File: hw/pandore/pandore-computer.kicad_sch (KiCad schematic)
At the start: 0 parts

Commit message: Added lots to sch and pcb: eth passive, audio codec, midi, teensy Corrected and added support for M.2
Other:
- sheet Computer module ports: added PCIEP0{PCIE1X}, PCIEP1{PCIE1X}, PCIEP2{PCIE1X}, PCIEP3{PCIE4X}, UART0{UART}, UART1{UART}, UART2{UART}; removed none
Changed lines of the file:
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@@
+		)
+	)
+	(wire
+		(pts
+			(xy 215.9 124.46) (xy 165.1 124.46)
+		)
+		(stroke
+			(width 0)
+			(type default)
 		)
 	)
@@
 		)
 	)
+	(wire
+		(pts
+			(xy 215.9 121.92) (xy 165.1 121.92)
+		)
+		(stroke
+			(width 0)
+			(type default)
+		)
+	)
 	(bus
 		(pts
@@
 		)
 	)
+	(wire
+		(pts
+			(xy 215.9 127) (xy 165.1 127)
+		)
+		(stroke
+			(width 0)
+			(type default)
+		)
+	)
+	(bus
+		(pts
+			(xy 92.71 140.97) (xy 121.92 140.97)
+		)
+		(stroke
+			(width 0)
+			(type default)
+		)
+	)
 	(bus
 		(pts
@@
 		)
 	)
+	(wire
+		(pts
+			(xy 215.9 119.38) (xy 165.1 119.38)
+		)
+		(stroke
+			(width 0)
+			(type default)
+		)
+	)
 	(bus
 		(pts
@@
 		(shape bidirectional)
 		(at 215.9 96.52 0)
+		(effects
+			(font
+				(size 1.016 1.016)
+			)
+			(justify left)
+		)
+	)
+	(hierarchical_label "M2E{PCIE1X}"
+		(shape bidirectional)
+		(at 215.9 121.92 0)
 		(effects
 			(font
@@
 		)
 	)
+	(hierarchical_label "ETHX{PCIE1X}"
+		(shape bidirectional)
+		(at 215.9 124.46 0)
+		(effects
+			(font
+				(size 1.016 1.016)
+			)
+			(justify left)
+		)
+	)
 	(hierarchical_label "DDIB{HDMI}"
 		(shape output)
@@
 		)
 	)
+	(hierarchical_label "MIDI{UART}"
+		(shape bidirectional)
+		(at 92.71 140.97 180)
+		(effects
+			(font
+				(size 1.016 1.016)
+			)
+			(justify right)
+		)
+	)
+	(hierarchical_label "M2M{PCIE4X}"
+		(shape bidirectional)
+		(at 215.9 127 0)
+		(effects
+			(font
+				(size 1.016 1.016)
+			)
+			(justify left)
+		)
+	)
 	(hierarchical_label "USBP1{USB3}"
 		(shape bidirectional)
 		(at 215.9 93.98 0)
+		(effects
+			(font
+				(size 1.016 1.016)
+			)
+			(justify left)
+		)
+	)
+	(hierarchical_label "ETHI{PCIE1X}"
+		(shape bidirectional)
+		(at 215.9 119.38 0)
 		(effects
 			(font
@@
 			)
 		)
+		(pin "PCIEP3{PCIE4X}" bidirectional
+			(at 165.1 127 0)
+			(effects
+				(font
+					(size 1.016 1.016)
+				)
+				(justify right)
+			)
+		)
+		(pin "PCIEP2{PCIE1X}" bidirectional
+			(at 165.1 124.46 0)
+			(effects
+				(font
+					(size 1.016 1.016)
+				)
+				(justify right)
+			)
+		)
+		(pin "PCIEP0{PCIE1X}" bidirectional
+			(at 165.1 119.38 0)
+			(effects
+				(font
+					(size 1.016 1.016)
+				)
+				(justify right)
+			)
+		)
+		(pin "PCIEP1{PCIE1X}" bidirectional
+			(at 165.1 121.92 0)
+			(effects
+				(font
+					(size 1.016 1.016)
+				)
+				(justify right)
+			)
+		)
+		(pin "UART2{UART}" bidirectional
+			(at 121.92 140.97 180)
+			(effects
+				(font
+					(size 1.016 1.016)
+				)
+				(justify left)
+			)
+		)
+		(pin "UART1{UART}" bidirectional
+			(at 165.1 73.66 0)
+			(effects
+				(font
+					(size 1.016 1.016)
+				)
+				(justify right)
+			)
+		)
+		(pin "UART0{UART}" bidirectional
+			(at 165.1 71.12 0)
+			(effects
+				(font
+					(size 1.016 1.016)
+				)
+				(justify right)
+			)
+		)

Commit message: added power stuff revised M.2 for higher model and added m.2 mounts added power tap terminals
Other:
- sheet Computer module ports: added I2S{I2S1DPX}; removed none
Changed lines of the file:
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@@
 	(bus
 		(pts
-			(xy 92.71 140.97) (xy 121.92 140.97)
+			(xy 92.71 149.86) (xy 121.92 149.86)
 		)
 		(stroke
@@
 	(bus
 		(pts
-			(xy 92.71 132.08) (xy 121.92 132.08)
+			(xy 92.71 147.32) (xy 121.92 147.32)
 		)
 		(stroke
@@
 		(pts
 			(xy 165.1 100.33) (xy 215.9 100.33)
+		)
+		(stroke
+			(width 0)
+			(type default)
+		)
+	)
+	(bus
+		(pts
+			(xy 92.71 152.4) (xy 121.92 152.4)
 		)
 		(stroke
@@
 		)
 	)
-	(hierarchical_label "MIDI{UART}"
-		(shape bidirectional)
-		(at 92.71 140.97 180)
+	(hierarchical_label "AUDIO.MIDI{UART}"
+		(shape bidirectional)
+		(at 92.71 149.86 180)
 		(effects
 			(font
@@
 		)
 	)
+	(hierarchical_label "AUDIO.I2S{I2S1DPX}"
+		(shape bidirectional)
+		(at 92.71 152.4 180)
+		(effects
+			(font
+				(size 1.016 1.016)
+			)
+			(justify right)
+		)
+	)
 	(hierarchical_label "ETHI{PCIE1X}"
 		(shape bidirectional)
@@
 		)
 	)
-	(hierarchical_label "USB2P6{USB2}"
-		(shape bidirectional)
-		(at 92.71 132.08 180)
+	(hierarchical_label "AUDIO.USB{USB2}"
+		(shape bidirectional)
+		(at 92.71 147.32 180)
 		(effects
 			(font
@@
 		)
 		(pin "USBP6{USB2}" bidirectional
-			(at 121.92 132.08 180)
+			(at 121.92 147.32 180)
 			(effects
 				(font
@@
 		)
 		(pin "UART2{UART}" bidirectional
-			(at 121.92 140.97 180)
+			(at 121.92 149.86 180)
 			(effects
 				(font
@@
 			)
 		)
+		(pin "I2S{I2S1DPX}" bidirectional
+			(at 121.92 152.4 180)
+			(effects
+				(font
+					(size 1.016 1.016)
+				)
+				(justify left)
+			)
+		)

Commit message: added i2s/i2c isolation for audio section
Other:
- sheet Computer module ports: added I2S{I2S1DPX ~{RST}}; removed I2S{I2S1DPX}
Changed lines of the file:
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@@
 		)
 	)
-	(hierarchical_label "AUDIO.I2S{I2S1DPX}"
+	(hierarchical_label "AUDIO.I2S{I2S1DPX ~{RST}}"
 		(shape bidirectional)
 		(at 92.71 152.4 180)
@@
 			)
 		)
-		(pin "I2S{I2S1DPX}" bidirectional
+		(pin "I2S{I2S1DPX ~{RST}}" bidirectional
 			(at 121.92 152.4 180)
 			(effects

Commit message: lots of routing (diff, buses, power) done optimised buffer out
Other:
- sheet Computer module ports: added I2C2{I2C}, I2C3{I2C}, I2C4{I2C}, I2C5{I2C}; removed none
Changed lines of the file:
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@@
+		)
+	)
+	(bus
+		(pts
+			(xy 165.1 146.05) (xy 215.9 146.05)
+		)
+		(stroke
+			(width 0)
+			(type default)
+		)
+	)
+	(bus
+		(pts
+			(xy 92.71 154.94) (xy 121.92 154.94)
+		)
+		(stroke
+			(width 0)
+			(type default)
 		)
 	)
@@
 	(wire
 		(pts
-			(xy 215.9 121.92) (xy 165.1 121.92)
+			(xy 215.9 143.51) (xy 165.1 143.51)
 		)
 		(stroke
@@
 	(hierarchical_label "M2E{PCIE1X}"
 		(shape bidirectional)
-		(at 215.9 121.92 0)
+		(at 215.9 143.51 0)
 		(effects
 			(font
@@
 		)
 	)
+	(hierarchical_label "AUDIO{I2C}"
+		(shape bidirectional)
+		(at 92.71 154.94 180)
+		(effects
+			(font
+				(size 1.016 1.016)
+			)
+			(justify right)
+		)
+	)
 	(hierarchical_label "USB2P5{USB2}"
 		(shape bidirectional)
@@
 		(shape output)
 		(at 215.9 88.9 0)
+		(effects
+			(font
+				(size 1.016 1.016)
+			)
+			(justify left)
+		)
+	)
+	(hierarchical_label "M2E{I2C}"
+		(shape bidirectional)
+		(at 215.9 146.05 0)
 		(effects
 			(font
@@
 		)
 		(pin "PCIEP1{PCIE1X}" bidirectional
-			(at 165.1 121.92 0)
+			(at 165.1 143.51 0)
 			(effects
 				(font
@@
 		)
 		(pin "UART1{UART}" bidirectional
-			(at 165.1 73.66 0)
+			(at 165.1 67.31 0)
 			(effects
 				(font
@@
 		)
 		(pin "UART0{UART}" bidirectional
-			(at 165.1 71.12 0)
+			(at 165.1 64.77 0)
 			(effects
 				(font
@@
 			)
 		)
+		(pin "I2C2{I2C}" bidirectional
+			(at 121.92 154.94 180)
+			(effects
+				(font
+					(size 1.016 1.016)
+				)
+				(justify left)
+			)
+		)
+		(pin "I2C5{I2C}" bidirectional
+			(at 165.1 146.05 0)
+			(effects
+				(font
+					(size 1.016 1.016)
+				)
+				(justify right)
+			)
+		)
+		(pin "I2C3{I2C}" bidirectional
+			(at 165.1 71.12 0)
+			(effects
+				(font
+					(size 1.016 1.016)
+				)
+				(justify right)
+			)
+		)
+		(pin "I2C4{I2C}" bidirectional
+			(at 165.1 73.66 0)
+			(effects
+				(font
+					(size 1.016 1.016)
+				)
+				(justify right)
+			)
+		)

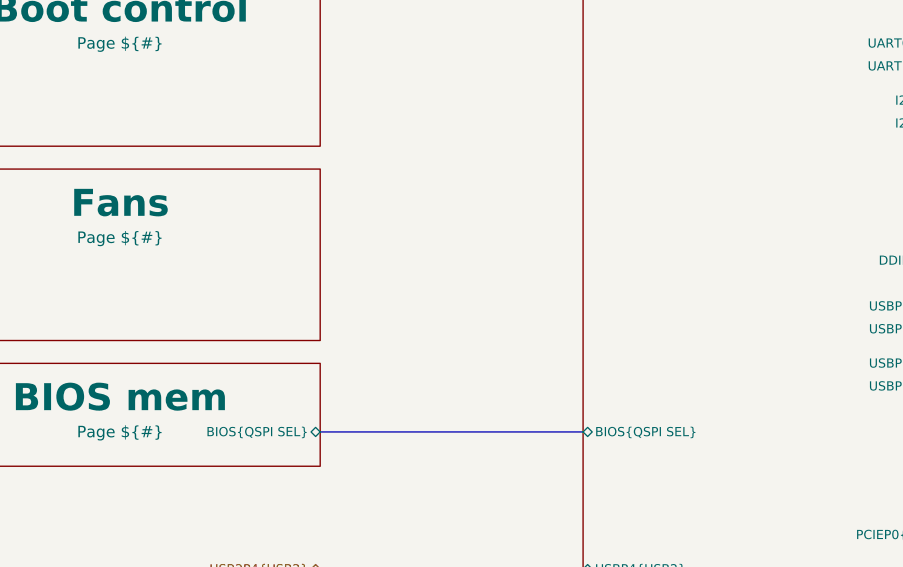
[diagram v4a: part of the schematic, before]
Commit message: lcd control circuit added fan interface added rgba output pinout for management mcu accessories done
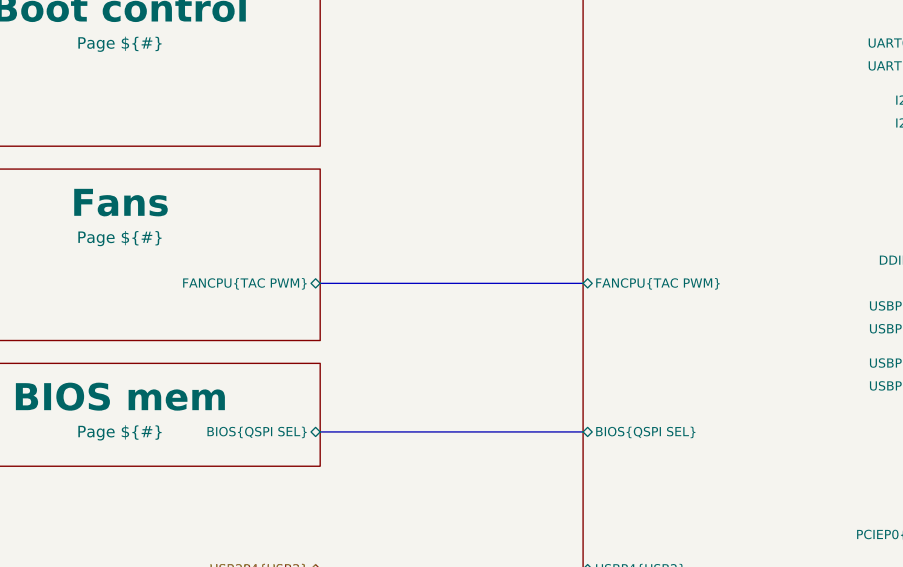
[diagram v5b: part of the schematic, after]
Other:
- sheet Computer module ports: added FANCPU{TAC PWM}; removed none
- sheet Fans ports: added FANCPU{TAC PWM}; removed none
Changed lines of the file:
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@@
+	(bus
+		(pts
+			(xy 92.71 91.44) (xy 121.92 91.44)
+		)
+		(stroke
+			(width 0)
+			(type default)
+		)
+	)
 	(bus
 		(pts
@@
 			)
 		)
+		(pin "FANCPU{TAC PWM}" bidirectional
+			(at 121.92 91.44 180)
+			(effects
+				(font
+					(size 1.016 1.016)
+				)
+				(justify left)
+			)
+		)
 		(instances
 			(project "pandore"
@@
 			)
 		)
+		(pin "FANCPU{TAC PWM}" bidirectional
+			(at 92.71 91.44 0)
+			(effects
+				(font
+					(size 1.016 1.016)
+				)
+				(justify right)
+			)
+		)

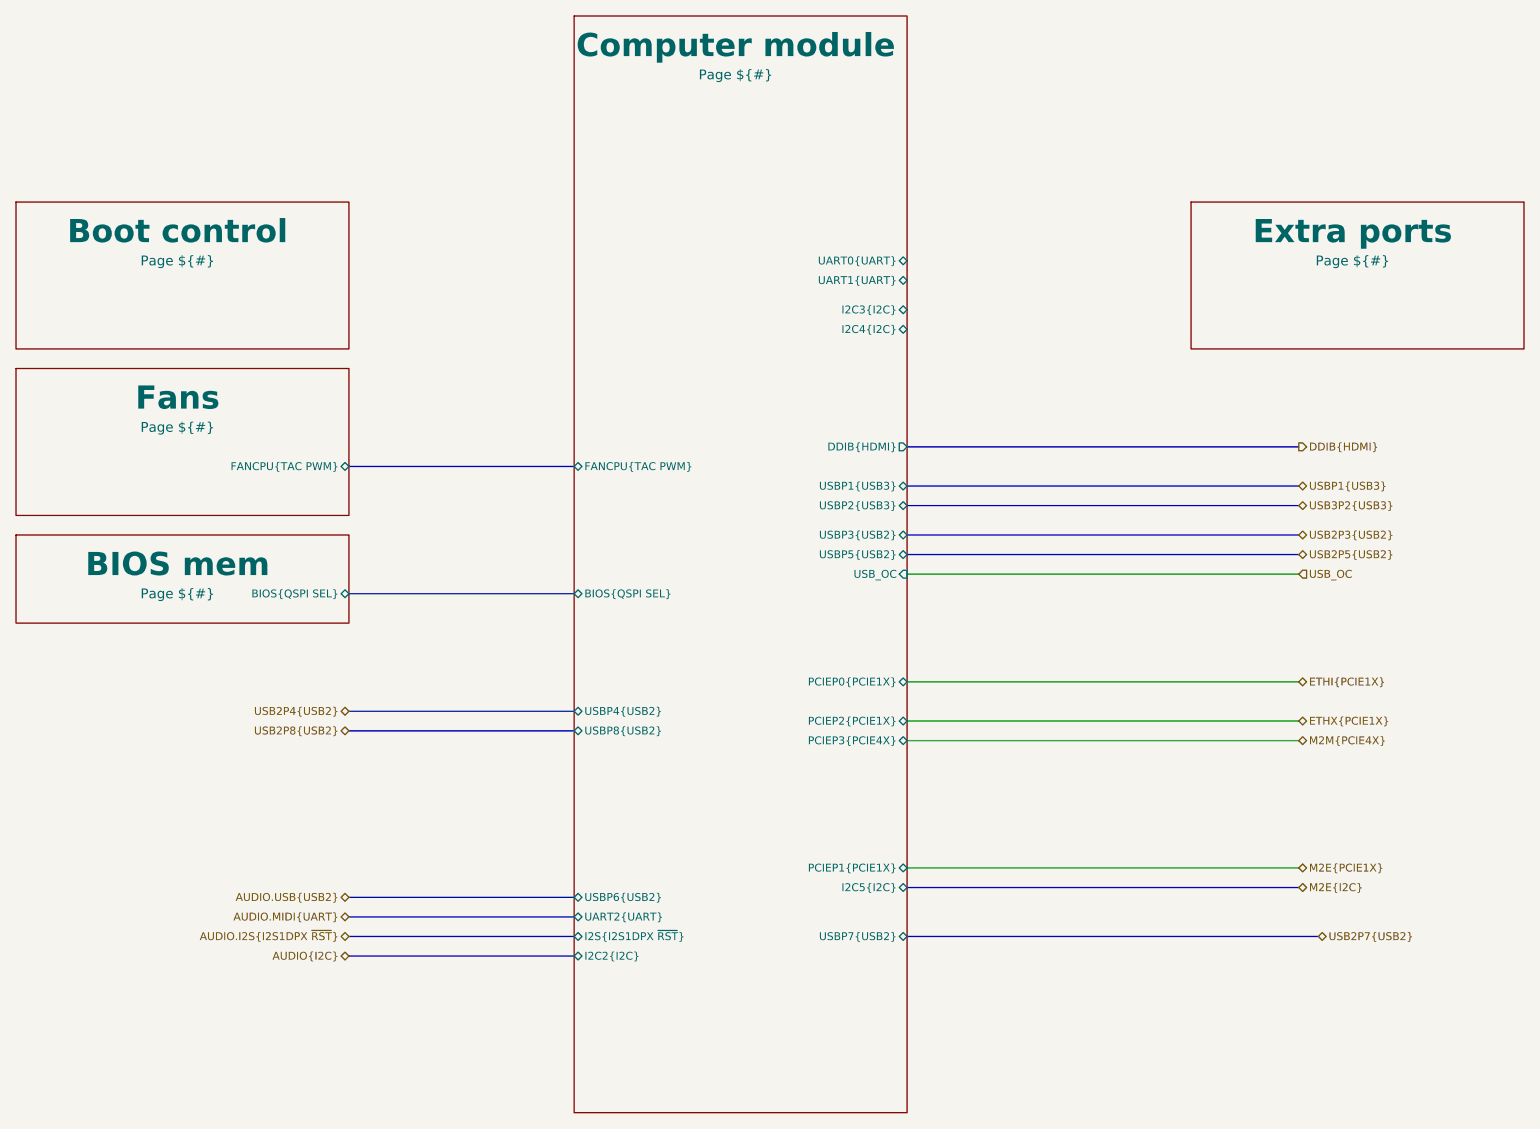
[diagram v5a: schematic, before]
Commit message: most of board control signals added, routed and defined
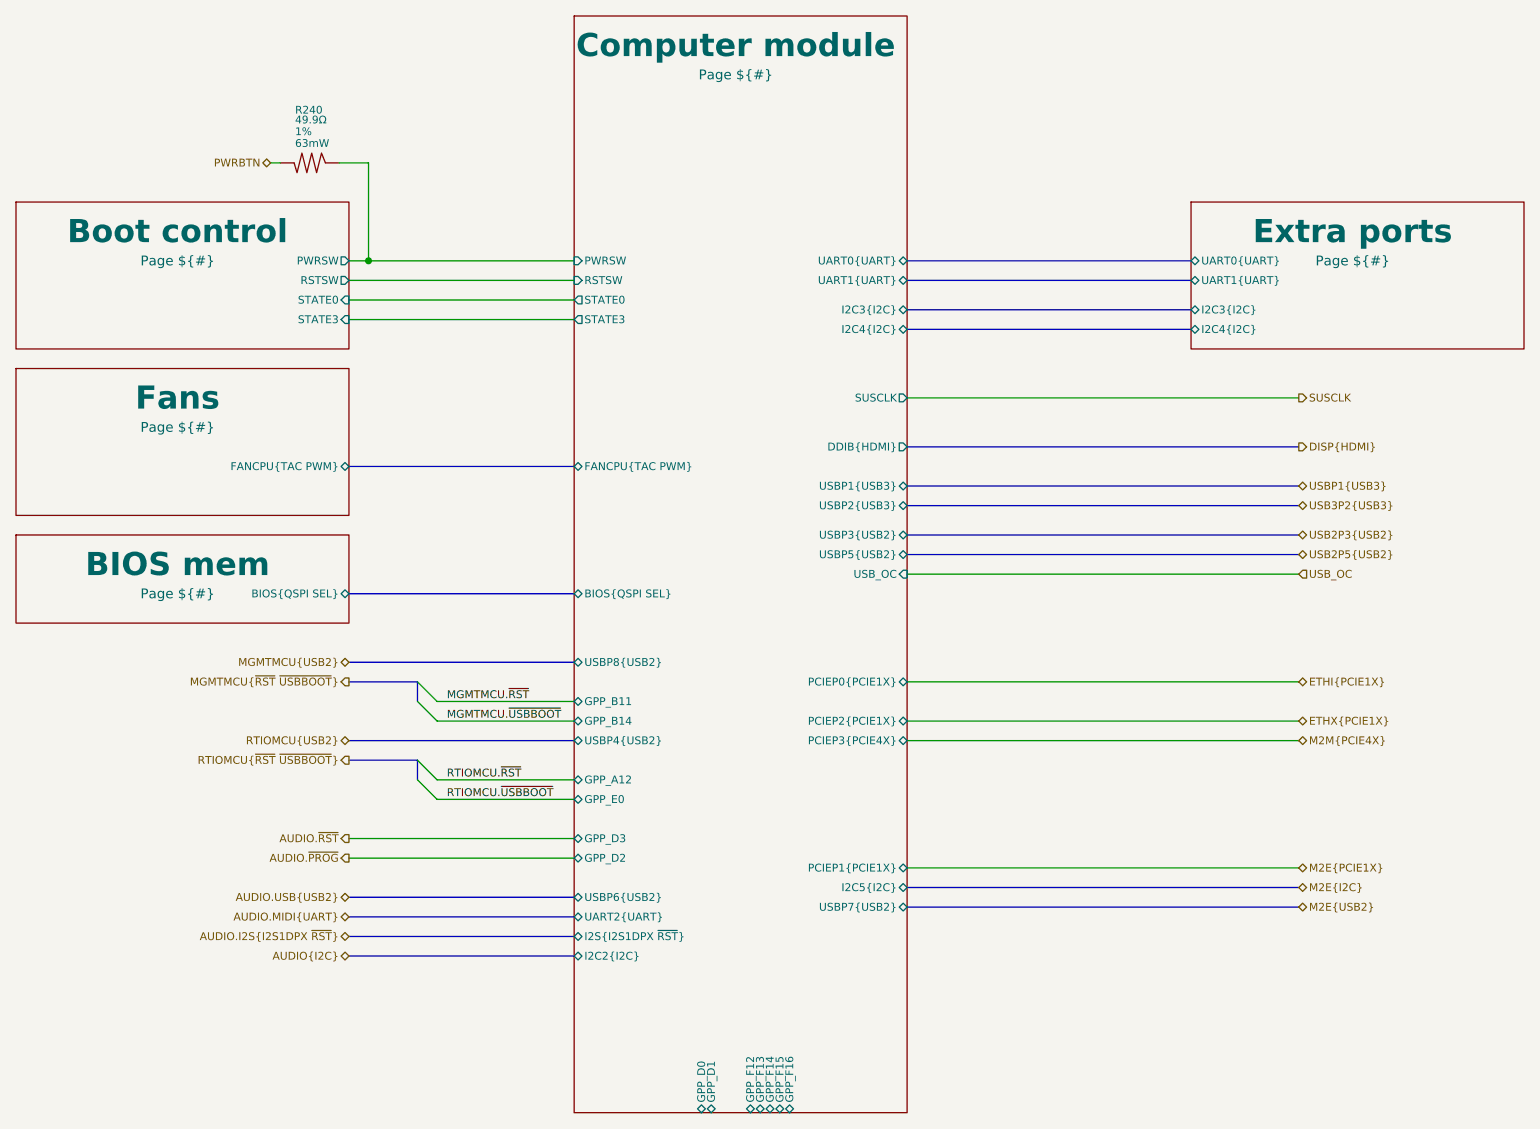
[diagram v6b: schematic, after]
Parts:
- added R240: ${Resistance}, ${Tolerance}, ${Power}, reekilib_res:RESC1005, symbol reekilib_res:res
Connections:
- new net Boot control/PWRSW: R240.2
- new net PWRBTN: R240.1
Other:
- sheet Boot control ports: added PWRSW, RSTSW, STATE0, STATE3; removed none
- sheet Computer module ports: added GPP_A12, GPP_B11, GPP_B14, GPP_D0, GPP_D1, GPP_D2, GPP_D3, GPP_E0, GPP_F12, GPP_F13, GPP_F14, GPP_F15, GPP_F16, PWRSW, RSTSW, STATE0, STATE3, SUSCLK; removed none
- sheet Extra ports ports: added I2C3{I2C}, I2C4{I2C}, UART0{UART}, UART1{UART}; removed none

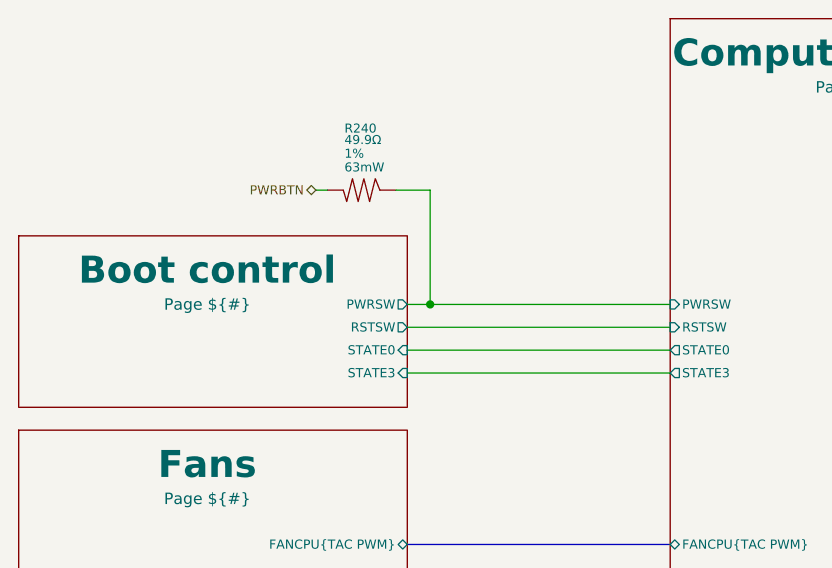
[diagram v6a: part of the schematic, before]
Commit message: added expansion port and more ctl to rp2350s routing much progress
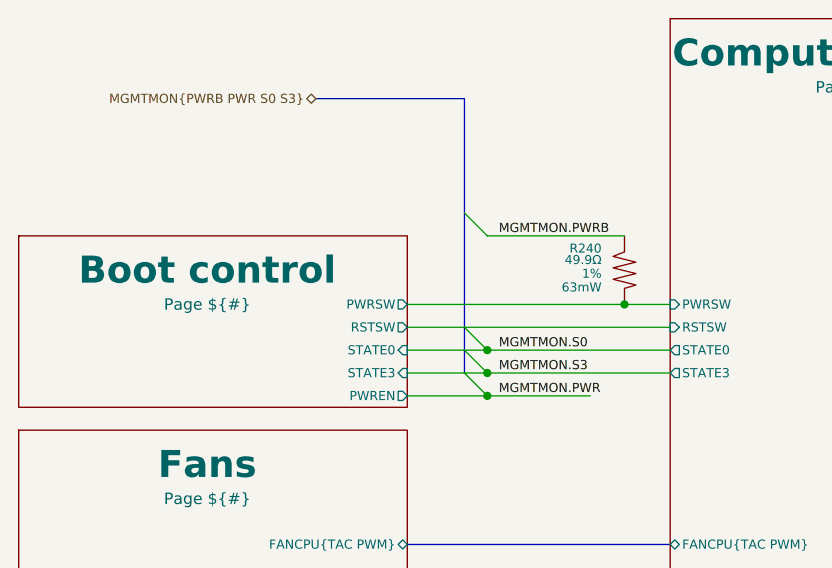
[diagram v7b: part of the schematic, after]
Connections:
- net PWRBTN is gone; now on net Boot control/PWRSW: R240.1
- net Boot control/PWRSW: no longer R240.2
- new net MGMTMON.PWRB: R240.2
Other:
- sheet Boot control ports: added PWREN; removed none
- moved on the sheet: R240
